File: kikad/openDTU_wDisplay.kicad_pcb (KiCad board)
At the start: 2 copper layers, 96 x 31 mm, 13 parts

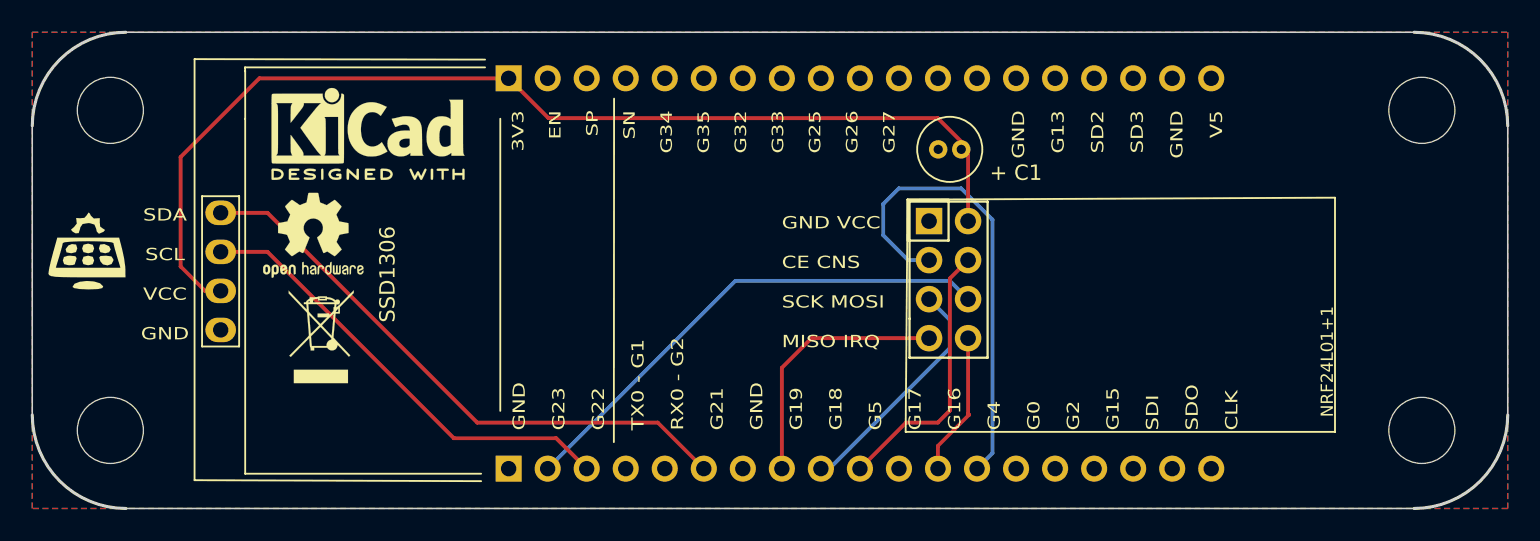
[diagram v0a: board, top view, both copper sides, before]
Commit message: add support for NRF with external antenna shrink photos
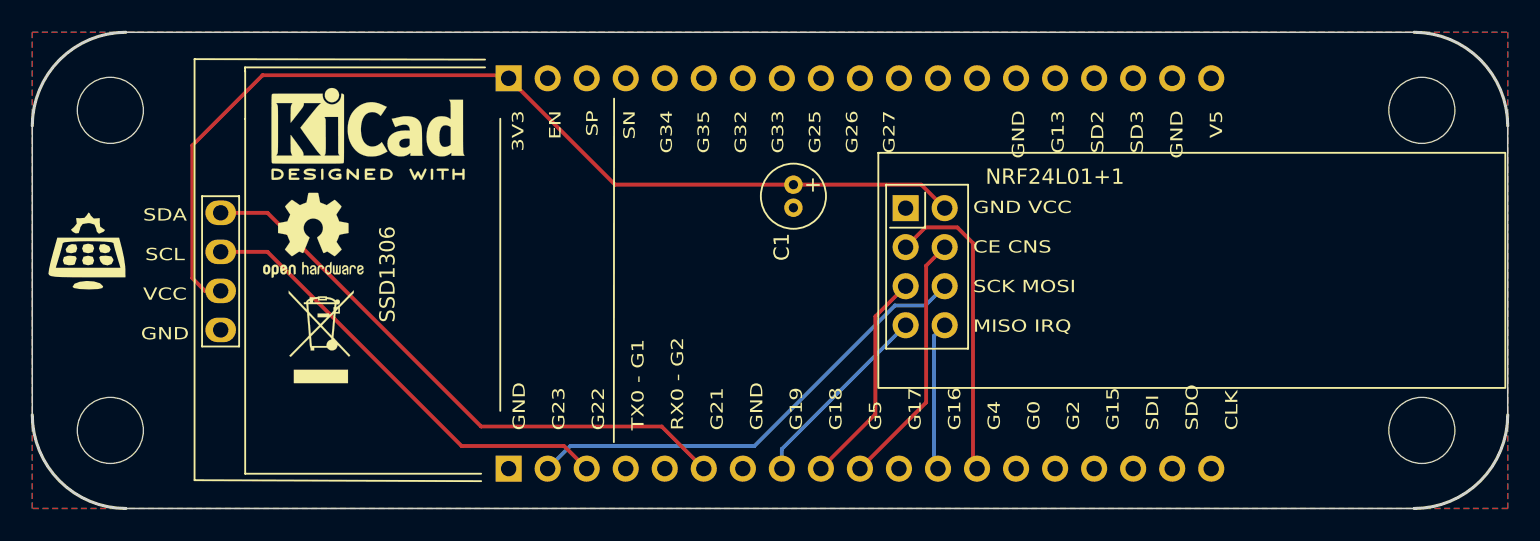
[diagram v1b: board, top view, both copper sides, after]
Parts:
- C1: renamed from + C1
- NRF24L01+1: footprint special:NRF24L01 -> nRF24L01+PA+LNA_Breakout:nRF24L01+PA+LNA_Breakout
- moved C1 11.2 mm to (139.4, 79.5), turned to -90 degrees
- moved NRF24L01+1 0.68 mm to (146.7, 81.0), turned to 0 degrees
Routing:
- net CE: track 30.7 -> 20.1 mm
- net PWR3x3: track 70.4 -> 65.3 mm
- net MISO: track 16.9 -> 12.7 mm
- net MOSI: track 32.9 -> 30.8 mm
- net SCK: track 15.4 -> 14.2 mm
- net ~{CSN}: track 17.7 -> 16.7 mm
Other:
- board text added: "+"
- board text added: "VCC GND CNS CE MOSI SCK IRQ MISO"
